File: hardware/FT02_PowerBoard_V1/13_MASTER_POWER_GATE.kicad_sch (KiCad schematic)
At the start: 10 parts, among them J1301 PWR_SW: ON / COMMON / OFF, U1301 TPS22953DQCR CANDIDATE

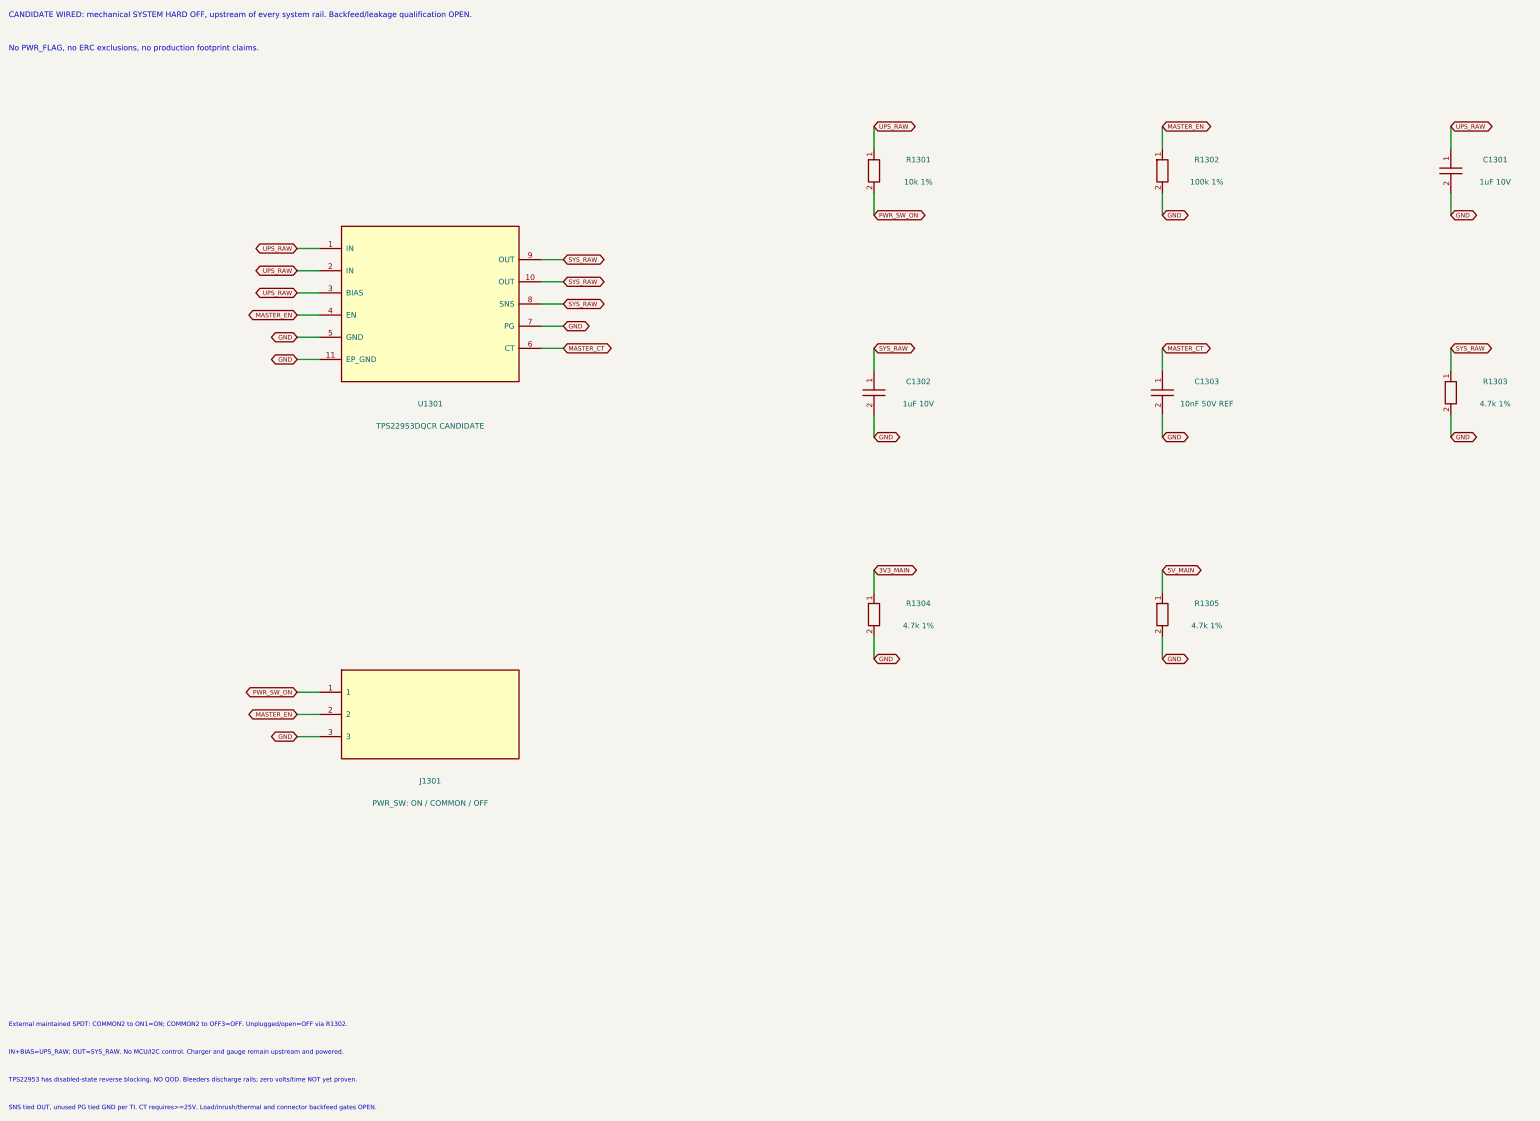
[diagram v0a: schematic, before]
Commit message: Add mechanically selected FT02 rail discharge and OVP feasibility checks
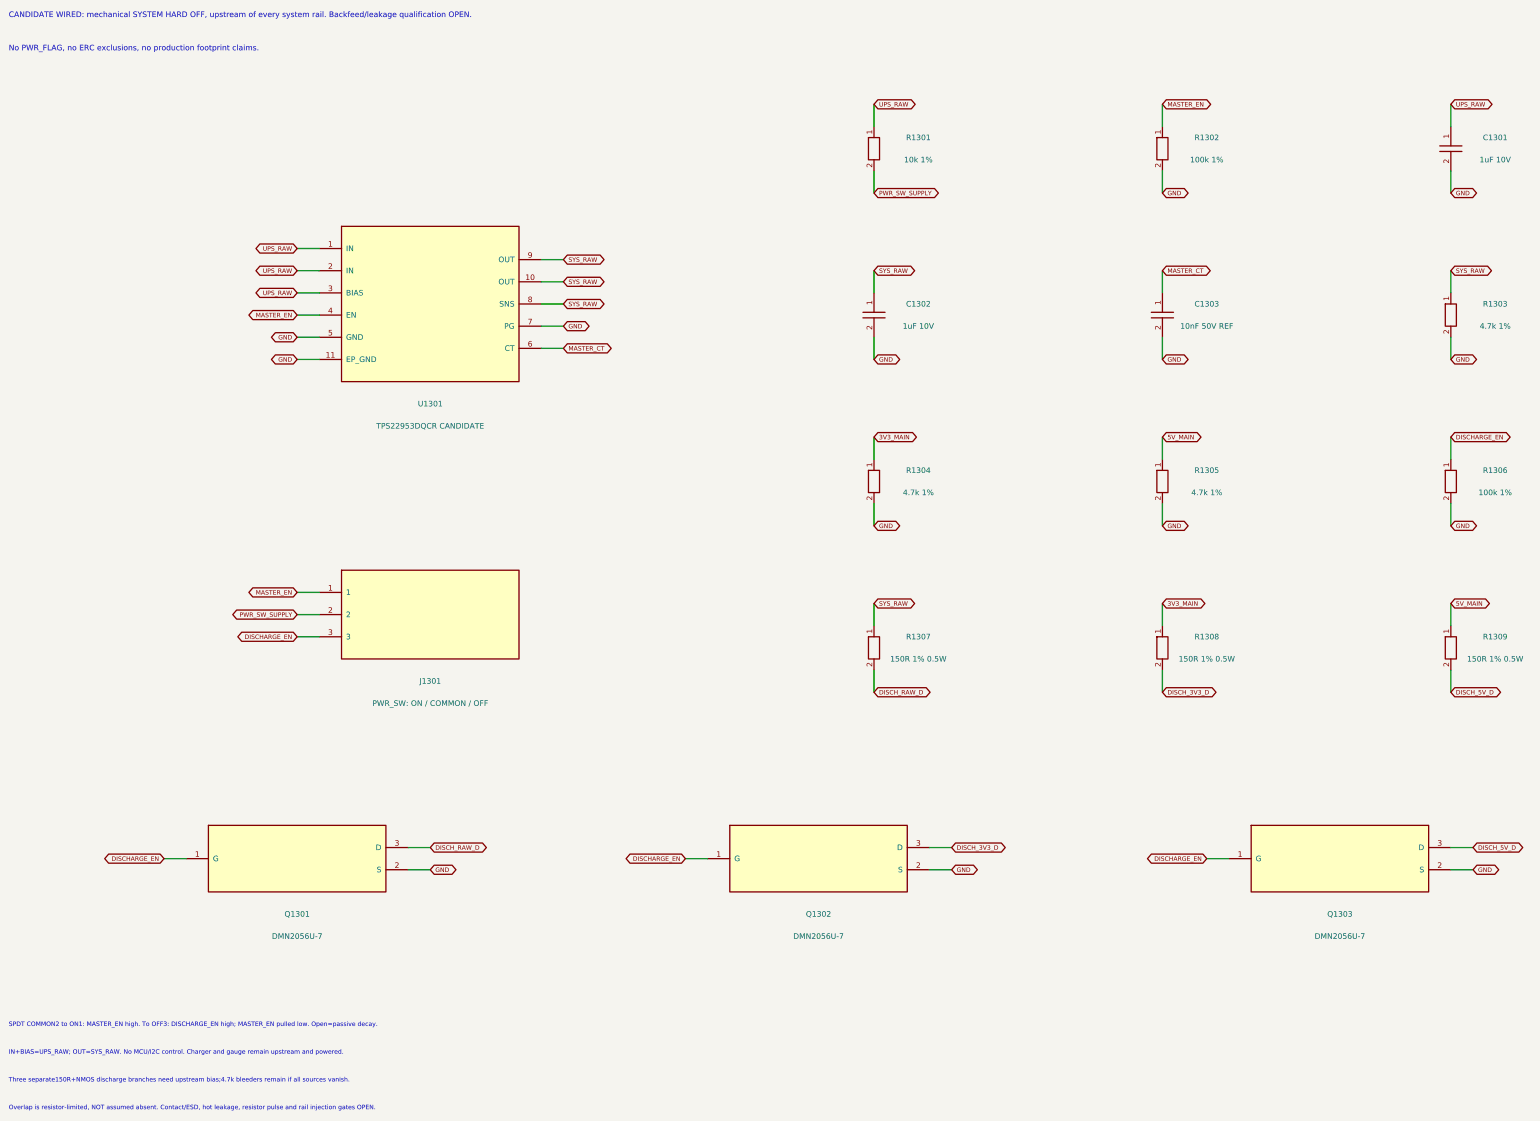
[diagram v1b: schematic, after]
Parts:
- added Q1301, Q1302, Q1303: DMN2056U-7, symbol FT02_Reference:DMN2056U
- added R1306: 100k 1%, symbol FT02_Reference:R
- added R1307, R1308, R1309: 150R 1% 0.5W, symbol FT02_Reference:R
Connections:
- net 3V3_MAIN: now also R1308.1
- net 5V_MAIN: now also R1309.1
- net GND: now also Q1301.2 (S), Q1302.2 (S), Q1303.2 (S), R1306.2; no longer J1301.3
- net MASTER_EN: now also J1301.1; no longer J1301.2
- net SYS_RAW: now also R1307.1
- net PWR_SW_ON renamed PWR_SW_SUPPLY
- net PWR_SW_SUPPLY: now also J1301.2; no longer J1301.1
- new net DISCHARGE_EN: J1301.3, Q1301.1 (G), Q1302.1 (G), Q1303.1 (G), R1306.1
- new net DISCH_3V3_D: Q1302.3 (D), R1308.2
- new net DISCH_5V_D: Q1303.3 (D), R1309.2
- new net DISCH_RAW_D: Q1301.3 (D), R1307.2
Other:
- note added: "Overlap is resistor-limited, NOT assumed absent. Contact/ESD, hot leakage, resistor pulse and rail injection gates OPEN."
- note added: "SPDT COMMON2 to ON1: MASTER_EN high. To OFF3: DISCHARGE_EN high; MASTER_EN pulled low. Open=passive decay."
- note added: "Three separate150R+NMOS discharge branches need upstream bias;4.7k bleeders remain if all sources vanish."
- note removed: "External maintained SPDT: COMMON2 to ON1=ON; COMMON2 to OFF3=OFF. Unplugged/open=OFF via R1302."
- note removed: "SNS tied OUT, unused PG tied GND per TI. CT requires>=25V. Load/inrush/thermal and connector backfeed gates OPEN."
- note removed: "TPS22953 has disabled-state reverse blocking, NO QOD. Bleeders discharge rails; zero volts/time NOT yet proven."
- moved on the sheet: C1301, C1302, C1303, J1301, R1301, R1302, R1303, R1304, R1305
